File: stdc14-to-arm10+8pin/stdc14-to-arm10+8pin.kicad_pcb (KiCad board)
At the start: 2 copper layers, 26 x 41 mm, 4 parts, among them J1 Conn_ARM_JTAG_SWD_10, J2 Conn_ST_STDC14, J3 Conn_02x04_Counter_Clockwise

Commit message: prob fin?
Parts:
- removed REF**: CONN_soicProgSmall, swd-converter:SOIC_clipProgSmall
- added H1: MountingHole_Pad, MountingHole:MountingHole_2.7mm_M2.5_Pad, F.Cu at (105.5, 75.0)
- added H2: MountingHole_Pad, MountingHole:MountingHole_2.7mm_M2.5_Pad, F.Cu at (123.0, 92.5)
- added TP1: SWDIO, TestPoint:TestPoint_Pad_D1.0mm, B.Cu at (102.6, 94.0)
- added TP2: SWO, TestPoint:TestPoint_Pad_D1.0mm, B.Cu at (102.6, 96.0)
- added TP3: SWCLK, TestPoint:TestPoint_Pad_D1.0mm, B.Cu at (102.6, 98.0)
- added TP4: NRST, TestPoint:TestPoint_Pad_D1.0mm, B.Cu at (102.6, 100.0)
- added TP5: VCC, TestPoint:TestPoint_Pad_D1.0mm, B.Cu at (102.5, 82.0)
- added TP6: GND, TestPoint:TestPoint_Pad_D1.0mm, B.Cu at (102.5, 84.0)
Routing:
- net SWDIO: track 0.00 -> 49.8 mm, vias 0 -> 1
- net SWO: track 0.00 -> 42.7 mm
- net SWCLK: track 0.00 -> 39.3 mm, vias 0 -> 1
- net NRST: track 0.00 -> 32.8 mm, vias 0 -> 1
- net VCC: track 0.00 -> 21.6 mm, vias 0 -> 7
- net GND: track 0.00 -> 8.69 mm, vias 0 -> 5
- added copper zone on B.Cu, net GND
- added copper zone on F.Cu, net GND
- added copper zone on In1.Cu, net GND
- added copper zone on In3.Cu, net GND
- added copper zone on In2.Cu, net VCC
- added copper zone on In4.Cu, net VCC
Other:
- board size 26 x 41 mm -> 26 x 42.5 mm
- copper layers 2 -> 6
- board text added: "GND"
- board text added: "JLCJLCJLC"
- board text added: "NRST"
- board text added: "SWCLK"
- board text added: "SWDIO"
- board text added: "SWO"
- board text added: "VCC"
- board text removed: "SWDIO SWO SWCLK NRST"
- board text removed: "VCC - - GND"

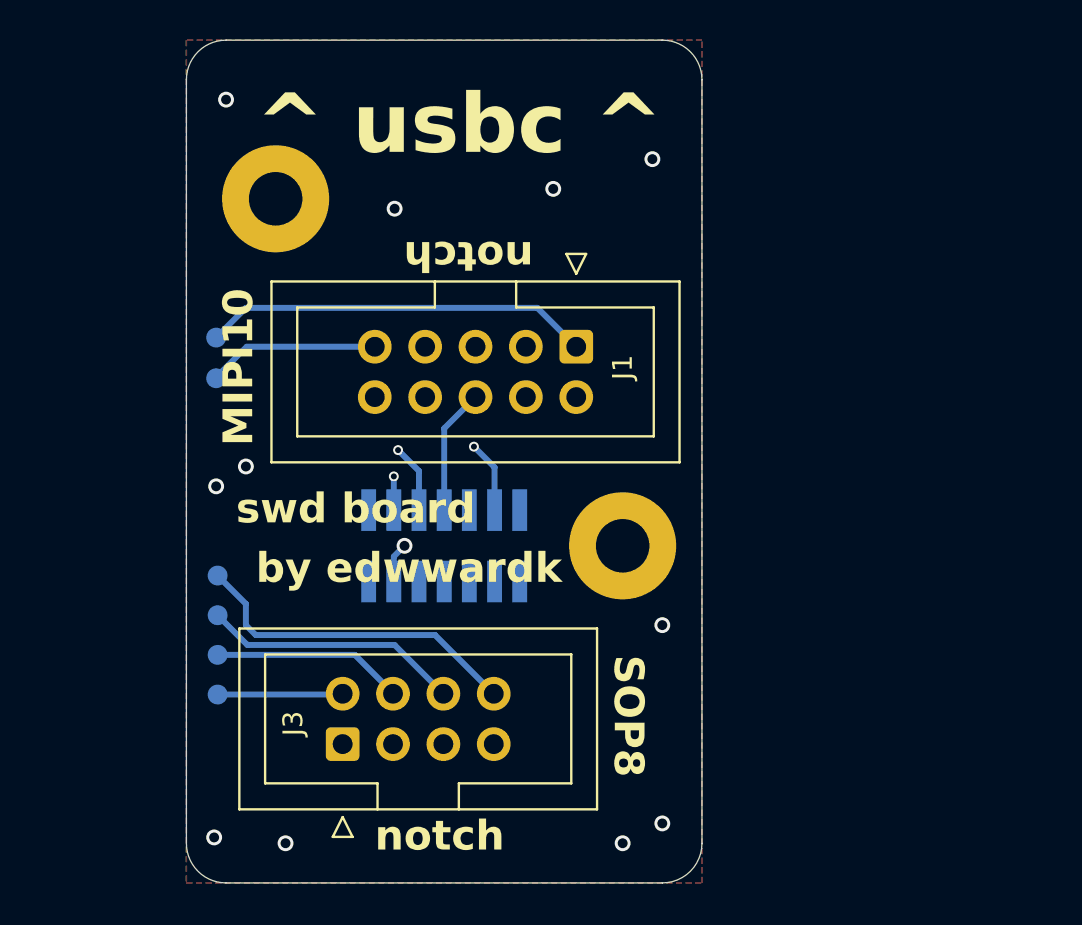
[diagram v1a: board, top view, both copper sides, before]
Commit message: moved some traces, add decoupling
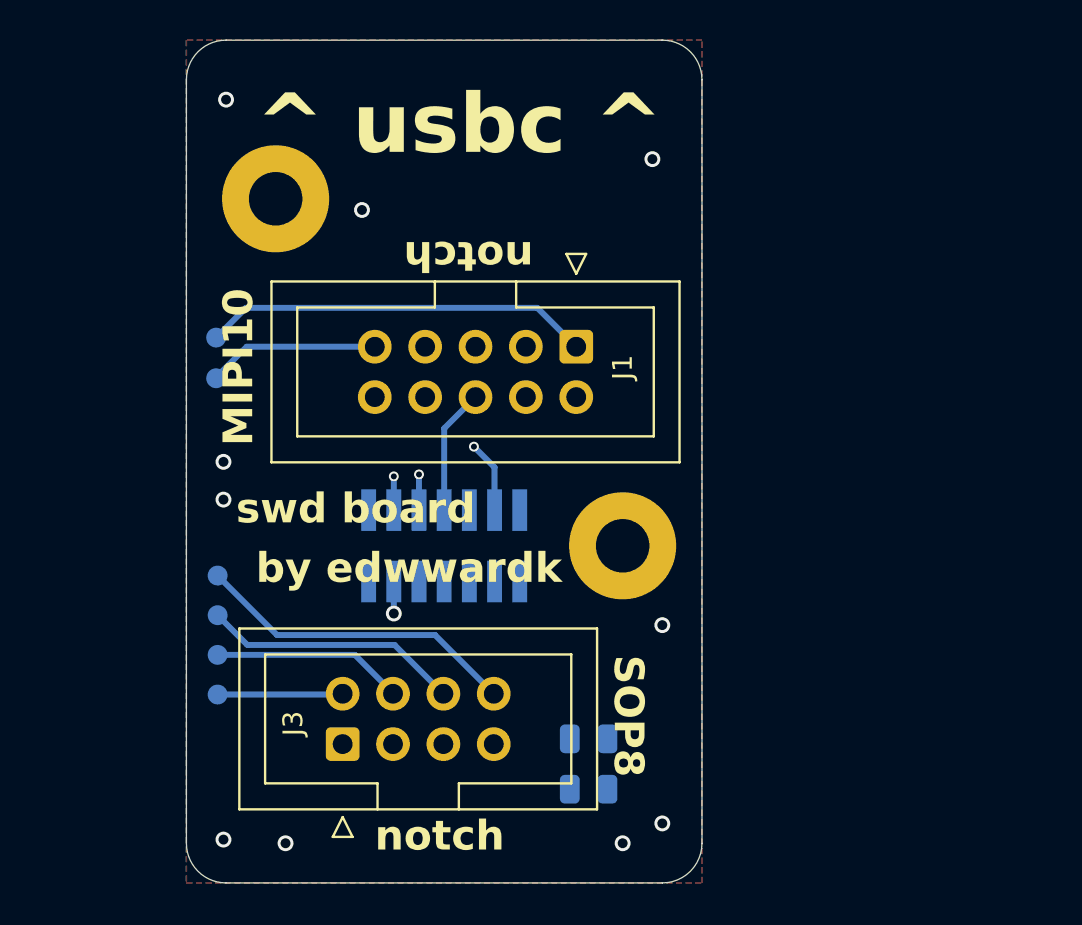
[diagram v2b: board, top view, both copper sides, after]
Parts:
- added C1: C, Capacitor_SMD:C_0805_2012Metric, B.Cu at (121.3, 104.8)
- added C2: C, Capacitor_SMD:C_0805_2012Metric, B.Cu at (121.3, 102.2)
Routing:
- net SWDIO: track 49.8 -> 40.6 mm
- net SWO: track 42.7 -> 35.0 mm
- net NRST: track 32.8 -> 35.0 mm
- net SWCLK: track 39.3 -> 37.5 mm
- net GND: vias 5 -> 4

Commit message: moved couple things
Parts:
- moved C1 26.8 mm to (120.0, 78.0)
- moved C2 26.8 mm to (120.0, 75.5)
- moved TP5 8.96 mm to (103.0, 91.0)
- moved TP6 8.96 mm to (103.0, 93.0)
- moved TP1 4.52 mm to (103.0, 98.5)
- moved TP2 4.52 mm to (103.0, 100.5)
- moved TP3 4.52 mm to (103.0, 102.5)
- moved TP4 4.52 mm to (103.0, 104.5)
- moved J3 4.03 mm to (112.9, 102.0)
- moved J2 1.30 mm to (114.0, 91.2)
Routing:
- net SWDIO: track 40.6 -> 17.0 mm
- net SWCLK: track 37.5 -> 17.6 mm
- net NRST: track 35.0 -> 15.5 mm
- net SWO: track 35.0 -> 15.6 mm, vias 0 -> 1
- net VCC: track 21.2 -> 2.39 mm, vias 7 -> 8
- net GND: track 8.69 -> 2.41 mm, vias 4 -> 5
- added copper zone on In2.Cu, net GND
- added copper zone on In4.Cu, net GND
- added copper zone on In3.Cu, net VCC
- removed copper zone on In3.Cu, net GND
- removed copper zone on In2.Cu, net VCC
- removed copper zone on In4.Cu, net VCC

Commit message: probably ready for manufacture
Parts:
- moved TP3 6.50 mm to (103.0, 96.0)
- moved TP4 5.50 mm to (103.0, 99.0)
- moved TP1 4.50 mm to (103.0, 103.0)
- moved J2 1.50 mm to (114.0, 92.7)
- moved C2 0.50 mm to (120.0, 75.0)
- moved TP2 0.50 mm to (103.0, 101.0)
- moved J3 0.46 mm to (112.9, 102.5)
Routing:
- net SWDIO: track 17.0 -> 45.5 mm, vias 1 -> 2
- net SWO: track 15.6 -> 39.1 mm
- net NRST: track 15.5 -> 32.1 mm, vias 1 -> 2
- net SWCLK: track 17.6 -> 33.9 mm, vias 1 -> 2
- net VCC: track 2.39 -> 13.5 mm, vias 8 -> 3
- net GND: vias 5 -> 6
- added copper zone on In3.Cu, net GND
- added copper zone on In4.Cu, net VCC
- removed copper zone on In4.Cu, net GND
- removed copper zone on In3.Cu, net VCC

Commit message: rev1
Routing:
- net VCC: track 13.5 -> 14.5 mm
- net NRST: track 32.1 -> 32.7 mm
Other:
- board text added: "JLCJLCJLCJLC"
- board text added: "rev1"
- board text removed: "JLCJLCJLC"
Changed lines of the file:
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@@
 			(layer "F.SilkS"
 				(type "Top Silk Screen")
+				(color "White")
 			)
 			(layer "F.Paste"
@@
 			(layer "F.Mask"
 				(type "Top Solder Mask")
+				(color "Green")
 				(thickness 0.01)
 			)
@@
 			(layer "B.Mask"
 				(type "Bottom Solder Mask")
+				(color "Green")
 				(thickness 0.01)
 			)
@@
 			(layer "B.SilkS"
 				(type "Bottom Silk Screen")
+				(color "White")
 			)
 			(copper_finish "ENIG")
@@
 		)
 	)
-	(gr_text "JLCJLCJLC"
-		(locked yes)
-		(at 110 107 180)
+	(gr_text "JLCJLCJLCJLC\n"
+		(at 109 107 180)
 		(layer "B.SilkS")
 		(effects
@@
 		)
 	)
+	(gr_text "rev1"
+		(at 115.5 91.5 0)
+		(layer "F.SilkS")
+		(effects
+			(font
+				(size 1.1 1.1)
+				(thickness 0.25)
+				(bold yes)
+			)
+			(justify left bottom)
+		)
+	)
 	(gr_text "MIPI10"
 		(locked yes)
@@
 	)
 	(via
-		(at 105.5 108)
+		(at 103.5 107.5)
 		(size 0.8)
 		(drill 0.5)
@@
 	)
 	(segment
-		(start 108.25 95.25)
-		(end 108.25 93.25)
+		(start 115.62 87.5)
+		(end 118.12 85)
 		(width 0.3)
 		(layer "F.Cu")
@@
 	)
 	(segment
-		(start 115.62 87.5)
-		(end 118.12 85)
+		(start 108.25 95.25)
+		(end 110.5 97.5)
 		(width 0.3)
 		(layer "F.Cu")
@@
 	(segment
 		(start 108.25 95.25)
-		(end 110.71 95.25)
+		(end 108.25 93.25)
 		(width 0.3)
 		(layer "F.Cu")
@@
 	)
 	(segment
-		(start 110.71 95.25)
+		(start 112.96 97.5)
 		(end 115.42 99.96)
 		(width 0.3)
@@
 		(net 4)
 	)
+	(segment
+		(start 110.5 97.5)
+		(end 112.96 97.5)
+		(width 0.3)
+		(layer "F.Cu")
+		(net 4)
+	)
 	(via
 		(at 114 87.5)
@@
 	)
 	(via
-		(at 109 97.5)
+		(at 108 98.5)
 		(size 0.5)
 		(drill 0.3)
@@
 	)
 	(segment
-		(start 111.5 89)
-		(end 110.5 88)
+		(start 110 96.5)
+		(end 110 90.5)
 		(width 0.3)
 		(layer "In2.Cu")
@@
 	)
 	(segment
-		(start 110 96.5)
-		(end 110 90.5)
+		(start 108 98.5)
+		(end 109.46 99.96)
 		(width 0.3)
 		(layer "In2.Cu")
@@
 	)
 	(segment
-		(start 109 97.5)
-		(end 111.46 99.96)
+		(start 111.5 89)
+		(end 110.5 88)
 		(width 0.3)
 		(layer "In2.Cu")
@@
 	)
 	(segment
-		(start 111.46 99.96)
-		(end 112.88 99.96)
+		(start 110 90.5)
+		(end 111.5 89)
 		(width 0.3)
 		(layer "In2.Cu")
@@
 	)
 	(segment
-		(start 110.5 88)
-		(end 110.5 85)
+		(start 108 98.5)
+		(end 110 96.5)
 		(width 0.3)
 		(layer "In2.Cu")
@@
 	)
 	(segment
-		(start 116 89)
-		(end 111.5 89)
+		(start 109.46 99.96)
+		(end 112.88 99.96)
 		(width 0.3)
 		(layer "In2.Cu")
@@
 	)
 	(segment
-		(start 110 90.5)
-		(end 111.5 89)
+		(start 110.5 88)
+		(end 110.5 85)
 		(width 0.3)
 		(layer "In2.Cu")
@@
 	)
 	(segment
-		(start 109 97.5)
-		(end 110 96.5)
+		(start 116 89)
+		(end 111.5 89)
 		(width 0.3)
 		(layer "In2.Cu")
@@
 	)
 	(segment
-		(start 107.5 99)
-		(end 103 99)
+		(start 116 89)
+		(end 116.5 89.5)
 		(width 0.3)
 		(layer "B.Cu")
@@
 	)
 	(segment
-		(start 116 89)
-		(end 116.5 89.5)
+		(start 107.5 99)
+		(end 103 99)
 		(width 0.3)
 		(layer "B.Cu")
@@
 	)
 	(segment
-		(start 109 97.5)
+		(start 108 98.5)
 		(end 107.5 99)
 		(width 0.3)
@@
 	)
 	(via
-		(at 110 97.5)
+		(at 110 98.5)
 		(size 0.5)
 		(drill 0.3)
@@
 	)
 	(segment
-		(start 111.42 94.5)
-		(end 111.42 96.08)
-		(width 0.3)
-		(layer "B.Cu")
-		(net 6)
-	)
-	(segment
 		(start 123.5 75.5)
 		(end 123 75)
@@
 	)
 	(segment
+		(start 110 98.5)
+		(end 111.42 97.08)
+		(width 0.3)
+		(layer "B.Cu")
+		(net 6)
+	)
+	(segment
 		(start 123.5 76.5)
 		(end 123.5 75.5)
@@
 	)
 	(segment
-		(start 104.05 90.95)
-		(end 103 90.95)
+		(start 111.42 97.08)
+		(end 111.42 94.5)
 		(width 0.3)
 		(layer "B.Cu")
@@
 	)
 	(segment
-		(start 111.42 96.08)
-		(end 110 97.5)
+		(start 104.05 90.95)
+		(end 103 90.95)
 		(width 0.3)
 		(layer "B.Cu")
@@
 	)
 	(segment
-		(start 111.5 97)
-		(end 107.5 101)
+		(start 112.5 97)
+		(end 108.5 101)
 		(width 0.3)
 		(layer "B.Cu")
@@
 	)
 	(segment
-		(start 117.96 97)
-		(end 111.5 97)
+		(start 108.5 101)
+		(end 103 101)
 		(width 0.3)
 		(layer "B.Cu")
@@
 	)
 	(segment
-		(start 107.5 101)
-		(end 103 101)
+		(start 117.96 97)
+		(end 112.5 97)
 		(width 0.3)
 		(layer "B.Cu")
@@
 		(hatch edge 0.5)
 		(connect_pads
-			(clearance 0.4)
+			(clearance 0.3)
 		)
-		(min_thickness 0.25)
+		(min_thickness 0.3)
 		(filled_areas_thickness no)
 		(fill yes
@@
 		(priority 1)
 		(connect_pads
-			(clearance 0.4)
+			(clearance 0.3)
 		)
-		(min_thickness 0.25)
+		(min_thickness 0.3)
 		(filled_areas_thickness no)
 		(fill yes
